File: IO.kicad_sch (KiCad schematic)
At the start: 36 parts

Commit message: Issue #6 fixed
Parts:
- added R?: 10k, symbol Device:R_Small
- added Z? (x2): MMSZ4679, symbol JRIX Diode:MMSZ4679
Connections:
- net 5V: now also Z?.1
- net GND: now also R?.1
- net 3V3: no longer names the net of D?.1 (K), D?.1 (K)
- net 3V3: now also R?.2, Z?.2
- new net: Z?.1, Z?.2
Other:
- note added: "2V"
- moved on the sheet: D?

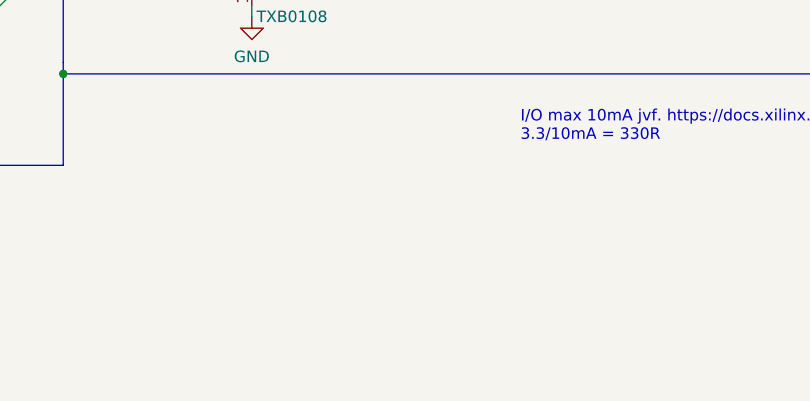
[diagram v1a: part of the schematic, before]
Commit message: Fixed issue #4 added more power pins
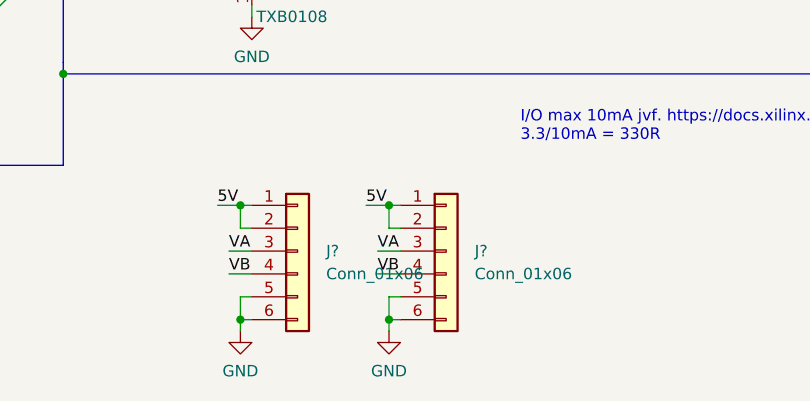
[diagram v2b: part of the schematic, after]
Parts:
- added J? (x2): Conn_01x06, symbol Connector_Generic:Conn_01x06
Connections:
- net 5V: now also J?.1 (Pin_1), J?.1 (Pin_1), J?.2 (Pin_2), J?.2 (Pin_2)
- net GND: now also J?.5 (Pin_5), J?.5 (Pin_5), J?.6 (Pin_6), J?.6 (Pin_6)
- net VA: now also J?.3 (Pin_3), J?.3 (Pin_3)
- net VB: now also J?.4 (Pin_4), J?.4 (Pin_4)

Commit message: Issue #5 and issue #6 fixed in schematic. Comprehensive PCB update required.
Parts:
- removed M?: Artix_7_35T_CMOD_A7, JRIX FPGA:CMOD A7 Module, symbol JRIX FPGA:Artix_7_35T_CMOD_A7
- added C? (x2): 100nF, Capacitor_SMD:C_0805_2012Metric_Pad1.18x1.45mm_HandSolder, symbol Device:C_Small
- added J?: Conn_01x08, symbol Connector_Generic:Conn_01x08
- added M? (x2): Artix_7_355_CMOD_A7_WCMOD, symbol JRIX FPGA:Artix_7_355_CMOD_A7_WCMOD
- added R? (x2): YC324, JRIX Resistor Array Footprints:YC-TC 124 8Pin-4R, symbol JRIX Resistor Array:YC324
- added U?: TXB0108, Package_SO:TSSOP-20_4.4x6.5mm_P0.65mm, symbol JRIX Level Translator:TXB0108
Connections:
- net 5V: no longer J?.2 (Pin_2), J?.2 (Pin_2)
- net 5VU_UNREG: now also M?.24 (VU)
- net AIN/NP15: now also M?.15 (AIN/NP15)
- net AIN/NP16: now also M?.16 (AIN/NP16)
- net GND: now also C?.2, C?.2, M?.25 (GND), M?.57 (CMGND1), M?.58 (CMGND2), U?.11 (GND)
- net VA: now also C?.1, U?.10 (OE), U?.2 (VCCA)
- net VB: now also C?.1, U?.19 (VCCB)
- net p1: now also M?.1 (PIO1)
- net p10: now also M?.10 (PIO10)
- net p11: now also M?.11 (PIO11)
- net p12: now also M?.12 (PIO12)
- net p13: now also M?.13 (PIO13)
- net p14: now also M?.14 (PIO14)
- net p17: now also M?.17 (PIO17)
- net p18: now also M?.18 (PIO18)
- net p19: now also M?.19 (PIO19)
- net p2: now also M?.2 (PIO2)
- net p20: now also M?.20 (PIO20)
- net p21: now also M?.21 (PIO21)
- net p22: now also M?.22 (PIO22)
- net p23: now also M?.23 (PIO23)
- net p26: now also M?.26 (PIO26)
- net p27: now also M?.27 (PIO27)
- net p28: now also M?.28 (PIO28)
- net p29: now also M?.29 (PIO29)
- net p3: now also M?.3 (PIO3)
- net p30: now also M?.30 (PIO30)
- net p31: now also M?.31 (PIO31)
- net p32: now also M?.32 (PIO32)
- net p33: now also M?.33 (PIO33)
- net p34: now also M?.34 (PIO34)
- net p35: now also M?.35 (PIO35)
- net p36: now also M?.36 (PIO36)
- net p37: now also M?.37 (PIO37)
- net p38: now also M?.38 (PIO38)
- net p39: now also M?.39 (PIO39)
- net p4: now also M?.4 (PIO4)
- net p40: now also M?.40 (PIO40)
- net p41: now also M?.41 (PIO41)
- net p42: now also M?.42 (PIO42)
- net p43: now also M?.43 (PIO43)
- net p44: now also M?.44 (PIO44)
- net p45: now also M?.45 (PIO45)
- net p46: now also M?.46 (PIO46)
- net p47: now also M?.47 (PIO47)
- net p48: now also M?.48 (PIO48)
- net p5: now also M?.5 (PIO5)
- net p6: now also M?.6 (PIO6)
- net p7: now also M?.7 (PIO7)
- net p8: now also M?.8 (PIO8)
- net p9: now also M?.9 (PIO9)
- new net: R?.1, U?.6 (A5)
- new net: R?.2, U?.7 (A6)
- new net: R?.3, U?.8 (A7)
- new net: R?.4, U?.9 (A8)
- new net: R?.1, U?.1 (A1)
- new net: R?.2, U?.3 (A2)
- new net: R?.3, U?.4 (A3)
- new net: R?.4, U?.5 (A4)
- new net CM3V3: J?.2 (Pin_2), J?.2 (Pin_2), M?.59 (CMVCC1), M?.60 (CMVCC2)
- new net pcm1: M?.49 (CM1), R?.8
- new net pcm2: M?.50 (CM2), R?.7
- new net pcm3: M?.51 (CM3), R?.6
- new net pcm4: M?.52 (CM4), R?.5
- new net pcm5: M?.53 (CM5), R?.8
- new net pcm6: M?.54 (CM6), R?.7
- new net pcm7: M?.55 (CM7), R?.6
- new net pcm8: M?.56 (CM8), R?.5
- new net pocm1: J?.1 (Pin_1), U?.20 (B1)
- new net pocm2: J?.2 (Pin_2), U?.18 (B2)
- new net pocm3: J?.3 (Pin_3), U?.17 (B3)
- new net pocm4: J?.4 (Pin_4), U?.16 (B4)
- new net pocm5: J?.5 (Pin_5), U?.15 (B5)
- new net pocm6: J?.6 (Pin_6), U?.14 (B6)
- new net pocm7: J?.7 (Pin_7), U?.13 (B7)
- new net pocm8: J?.8 (Pin_8), U?.12 (B8)
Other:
- note added: "CMOD Connections"
- moved on the sheet: J?

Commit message: PCB work 12/3
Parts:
- removed M? (x2): Artix_7_355_CMOD_A7_WCMOD, symbol JRIX FPGA:Artix_7_355_CMOD_A7_WCMOD
- added M1: Artix_7_355_CMOD_A7_WPMOD, JRIX FPGA:CMOD A7 Module With PMOD, symbol JRIX FPGA:Artix_7_355_CMOD_A7_WPMOD
- J1, J2: renamed from J?; footprint (none) -> Connector_PinHeader_2.54mm:PinHeader_1x06_P2.54mm_Vertical
- J3: renamed from J?; footprint (none) -> Connector_PinHeader_2.54mm:PinHeader_1x08_P2.54mm_Vertical
- R12: renamed from R?; footprint (none) -> Resistor_SMD:R_0805_2012Metric_Pad1.20x1.40mm_HandSolder
- Z1, Z2: renamed from Z?; footprint (none) -> Diode_SMD:D_SOD-123
- gave numbers to parts that had none: 40
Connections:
- net 5VU_UNREG: now also M1.24 (VU)
- net AIN/NP15: now also M1.15 (AIN/NP15)
- net AIN/NP16: now also M1.16 (AIN/NP16)
- net CM3V3: now also M1.59 (PMVCC1), M1.60 (PMVCC2)
- net GND: now also M1.25 (GND), M1.57 (PMGND1), M1.58 (PMGND2)
- net p1: now also M1.1 (PIO1)
- net p10: now also M1.10 (PIO10)
- net p11: now also M1.11 (PIO11)
- net p12: now also M1.12 (PIO12)
- net p13: now also M1.13 (PIO13)
- net p14: now also M1.14 (PIO14)
- net p17: now also M1.17 (PIO17)
- net p18: now also M1.18 (PIO18)
- net p19: now also M1.19 (PIO19)
- net p2: now also M1.2 (PIO2)
- net p20: now also M1.20 (PIO20)
- net p21: now also M1.21 (PIO21)
- net p22: now also M1.22 (PIO22)
- net p23: now also M1.23 (PIO23)
- net p26: now also M1.26 (PIO26)
- net p27: now also M1.27 (PIO27)
- net p28: now also M1.28 (PIO28)
- net p29: now also M1.29 (PIO29)
- net p3: now also M1.3 (PIO3)
- net p30: now also M1.30 (PIO30)
- net p31: now also M1.31 (PIO31)
- net p32: now also M1.32 (PIO32)
- net p33: now also M1.33 (PIO33)
- net p34: now also M1.34 (PIO34)
- net p35: now also M1.35 (PIO35)
- net p36: now also M1.36 (PIO36)
- net p37: now also M1.37 (PIO37)
- net p38: now also M1.38 (PIO38)
- net p39: now also M1.39 (PIO39)
- net p4: now also M1.4 (PIO4)
- net p40: now also M1.40 (PIO40)
- net p41: now also M1.41 (PIO41)
- net p42: now also M1.42 (PIO42)
- net p43: now also M1.43 (PIO43)
- net p44: now also M1.44 (PIO44)
- net p45: now also M1.45 (PIO45)
- net p46: now also M1.46 (PIO46)
- net p47: now also M1.47 (PIO47)
- net p48: now also M1.48 (PIO48)
- net p5: now also M1.5 (PIO5)
- net p6: now also M1.6 (PIO6)
- net p7: now also M1.7 (PIO7)
- net p8: now also M1.8 (PIO8)
- net p9: now also M1.9 (PIO9)
- net pcm1 renamed pm1
- net pm1: now also M1.49 (PM1)
- net pcm2 renamed pm2
- net pm2: now also M1.50 (PM2)
- net pcm3 renamed pm3
- net pm3: now also M1.51 (PM3)
- net pcm4 renamed pm4
- net pm4: now also M1.52 (PM4)
- net pcm5 renamed pm5
- net pm5: now also M1.53 (PM5)
- net pcm6 renamed pm6
- net pm6: now also M1.54 (PM6)
- net pcm7 renamed pm7
- net pm7: now also M1.55 (PM7)
- net pcm8 renamed pm8
- net pm8: now also M1.56 (PM8)
- net pocm1 renamed pom1
- net pocm2 renamed pom2
- net pocm3 renamed pom3
- net pocm4 renamed pom4
- net pocm5 renamed pom5
- net pocm6 renamed pom6
- net pocm7 renamed pom7
- net pocm8 renamed pom8
